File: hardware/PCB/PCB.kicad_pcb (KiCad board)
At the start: 2 copper layers, 83.8 x 25.5 mm, 35 parts, among them J1 USB_C_Receptacle_USB2.0_16P, J2 Conn_01x05_Socket, SW1 SW_Push, SW2 SW_Push, SW3 SW_Push, U1 ESP32-S3-WROOM-1, U2 TPD4E02B04DQA, U3 SX1262 Core, U4 TPS63802DLAR

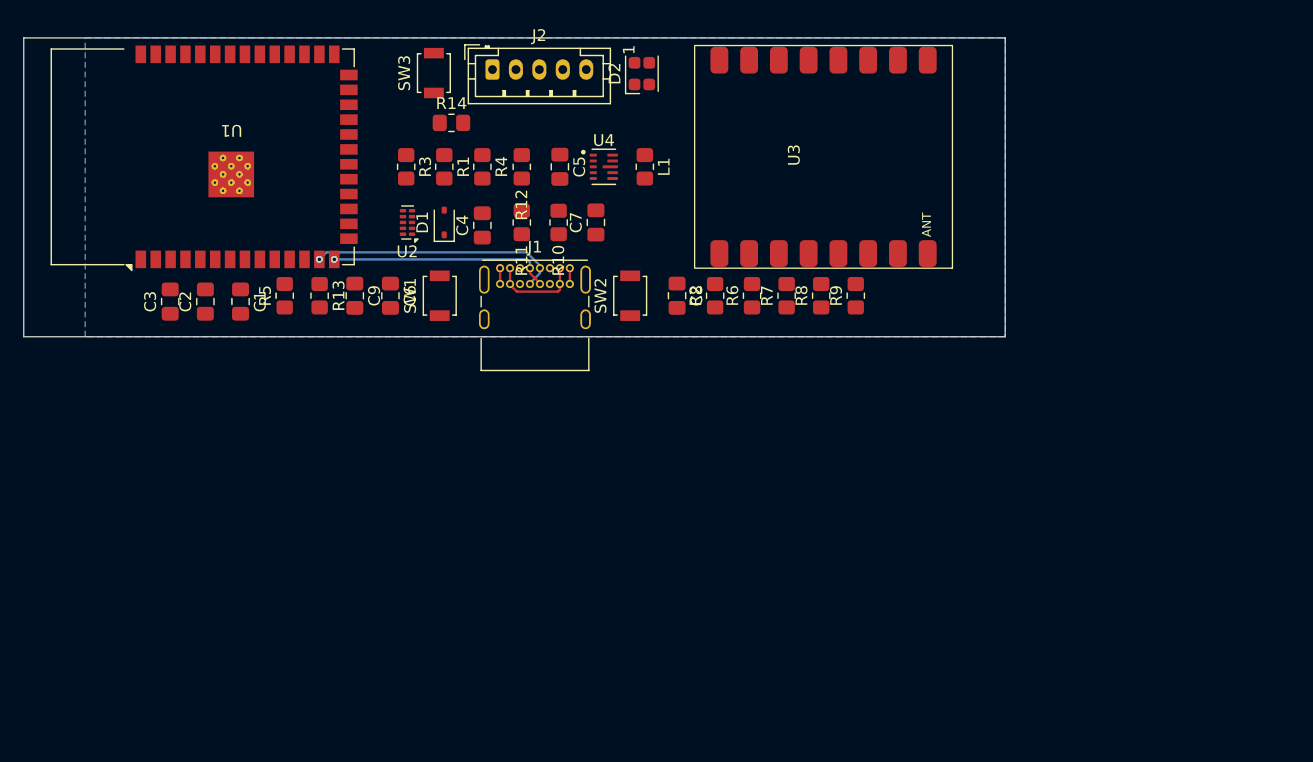
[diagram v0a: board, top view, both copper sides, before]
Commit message: feat: més versions de PCB i layouts inicials
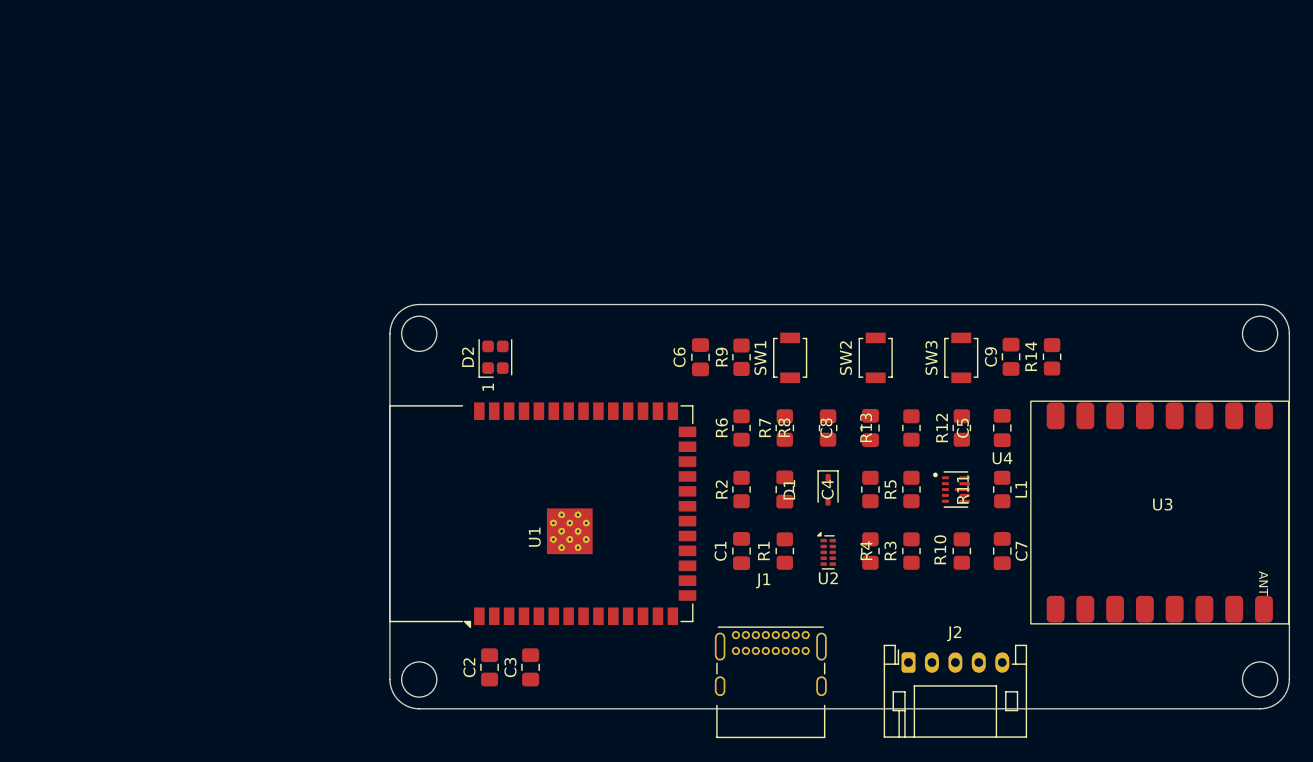
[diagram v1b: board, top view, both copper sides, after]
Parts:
- J2: footprint Connector_JST:JST_PH_B5B-PH-K_1x05_P2.00mm_Vertical -> Connector_JST:JST_PH_S5B-PH-K_1x05_P2.00mm_Horizontal
- moved J2 61.8 mm to (103.0, 158.1)
- moved C9 56.2 mm to (111.8, 132.0), turned to 90 degrees
- moved R14 55.0 mm to (115.2, 132.0), turned to -90 degrees
- moved R5 52.6 mm to (99.8, 143.3)
- moved R13 51.7 mm to (103.2, 138.0)
- moved R3 51.4 mm to (99.8, 148.5), turned to 90 degrees
- moved SW3 51.1 mm to (107.5, 132.1)
- moved R4 49.1 mm to (103.2, 148.5), turned to 90 degrees
- moved C1 47.8 mm to (88.8, 148.5)
- moved U2 45.6 mm to (96.1, 148.7), turned to 0 degrees
- moved C7 44.6 mm to (111.0, 148.5), turned to -90 degrees
- moved R10 44.4 mm to (107.5, 148.5), turned to 90 degrees
- moved C5 43.8 mm to (111.0, 138.0), turned to 90 degrees
- moved C3 43.8 mm to (70.8, 158.5)
- moved R1 43.8 mm to (92.4, 148.5)
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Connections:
- C1 pad 1: Net-(U1-EN) -> CHIP_PU
- R2 pad 2: Net-(U1-EN) -> CHIP_PU
- U1 pad 3: Net-(U1-EN) -> CHIP_PU
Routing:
- net data-: track 21.5 -> 0.00 mm, vias 1 -> 0
- net data+: track 19.0 -> 0.00 mm, vias 1 -> 0
- net Net-(D1-A): track 7.82 -> 0.00 mm
- net GND: track 2.70 -> 0.00 mm
- removed copper zone on B.Cu, net GND
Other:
- board size 83.8 x 25.5 mm -> 76.8 x 34.5 mm
